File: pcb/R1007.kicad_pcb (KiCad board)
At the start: 4 copper layers, 69 x 38.6 mm, 36 parts, among them J1 CONN500P-01X08, J2 CONN500P-01X08, J3 CONN_R1000A_EXTENSION, Q1 PSMN1R2-30YLC, Q2 PSMN1R2-30YLC, Q3 PSMN1R2-30YLC, Q4 PSMN1R2-30YLC, U1 74HC125, U2 AS78L05ZTR-E1, U3 TLP293-4

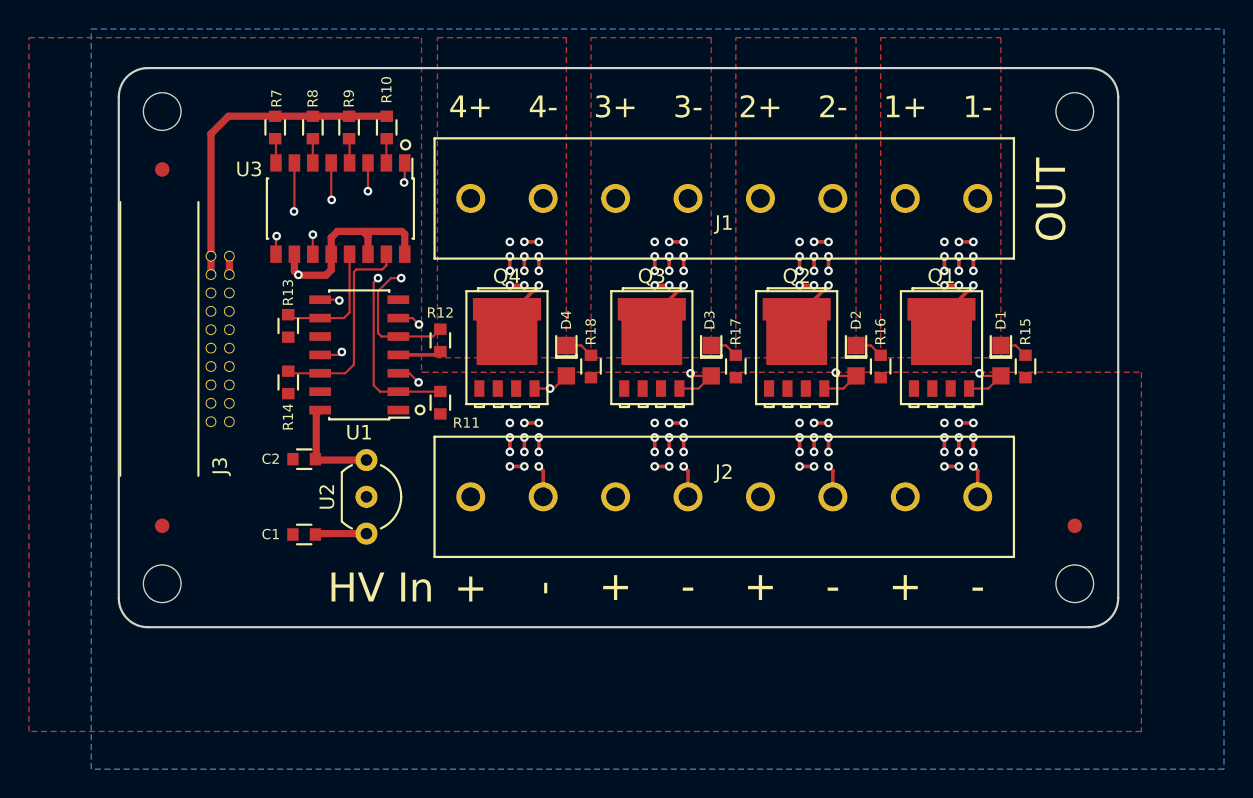
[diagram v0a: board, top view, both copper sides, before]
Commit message: separated +ve supplies and moved LEDs to board edge
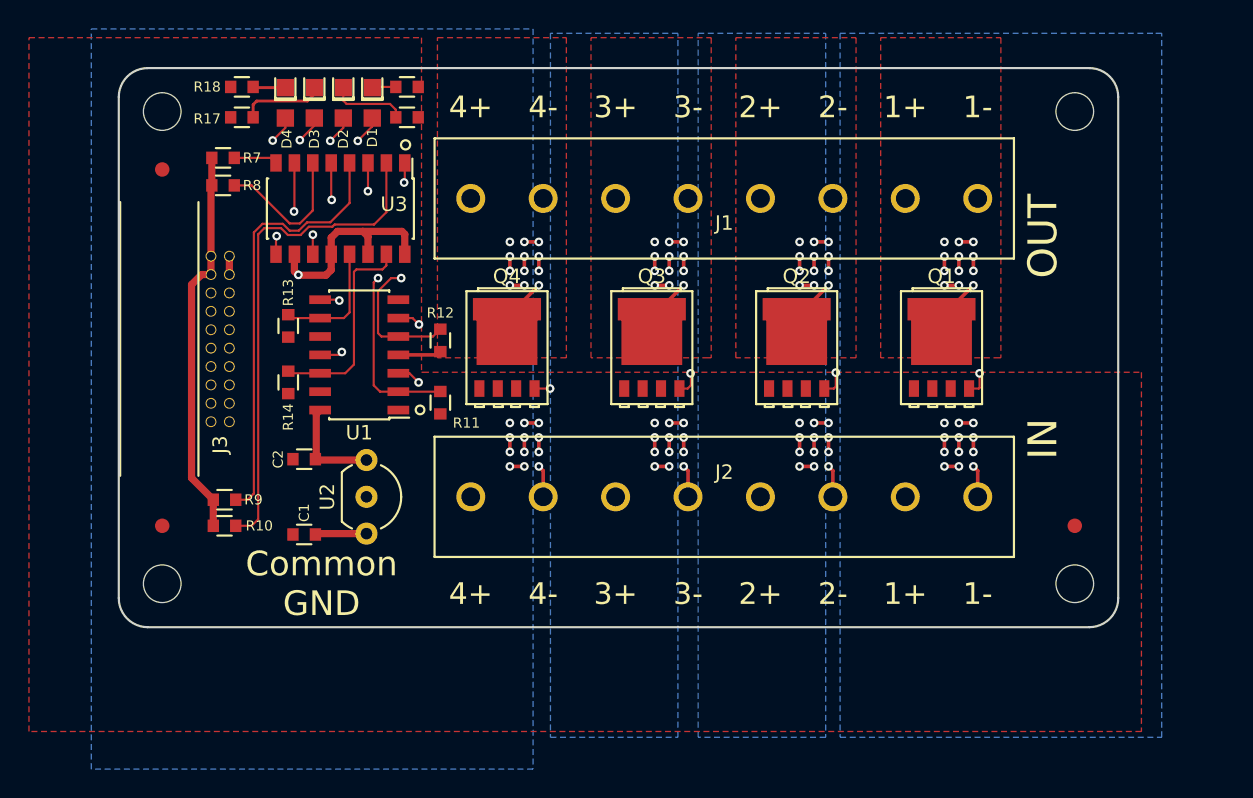
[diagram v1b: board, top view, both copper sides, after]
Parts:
- moved D1 46.9 mm to (120.5, 70.4)
- moved R15 46.9 mm to (122.9, 69.3), turned to 0 degrees
- moved D2 39.6 mm to (118.5, 70.4)
- moved R17 38.2 mm to (111.5, 71.4), turned to 180 degrees
- moved R16 36.9 mm to (122.9, 71.4), turned to 0 degrees
- moved D3 32.7 mm to (116.5, 70.4)
- moved R18 30.9 mm to (111.5, 69.3), turned to 180 degrees
- moved R10 29.7 mm to (110.3, 99.6), turned to 180 degrees
- moved R9 27.1 mm to (110.3, 97.8), turned to 180 degrees
- moved D4 26.3 mm to (114.5, 70.4)
- moved R8 7.38 mm to (110.2, 76.1), turned to 180 degrees
- moved R7 4.17 mm to (110.2, 74.2), turned to 180 degrees
- moved A1 3.00 mm to (159.4, 90.0)
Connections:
- J1 pad 2: VDD -> /VDD4
- J1 pad 4: VDD -> /VDD3
- J1 pad 6: VDD -> /VDD2
- J2 pad 3: VDD -> /VDD2
- J2 pad 5: VDD -> /VDD3
- J2 pad 7: VDD -> /VDD4
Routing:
- net /INR1: track 1.69 -> 34.7 mm
- net /INR2: track 1.69 -> 30.1 mm
- net /GN4: track 13.5 -> 39.4 mm, vias 2 -> 3
- net /GN3: track 28.2 -> 51.2 mm, vias 2 -> 3
- net /GN1: track 58.5 -> 73.2 mm, vias 2 -> 3
- net /GN2: track 43.2 -> 54.3 mm, vias 2 -> 3
- net /INR3: track 1.68 -> 10.2 mm
- net Net-(D3-Pad1): track 1.98 -> 5.85 mm
- net Net-(D2-Pad1): track 1.98 -> 5.31 mm
- net GND: track 25.0 -> 27.0 mm
- net /INR4: track 1.70 -> 3.03 mm
- added copper zone on B.Cu, net /VDD2
- added copper zone on In2.Cu, net /VDD2
- added copper zone on B.Cu, net /VDD3
- added copper zone on In2.Cu, net /VDD3
- added copper zone on B.Cu, net /VDD4
- added copper zone on In2.Cu, net /VDD4
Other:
- board text added: "Common GND"
- board text added: "IN"
- board text added: "R1007 v1.2 Quad 20A NFET Drivers plugg.ee Labs LLC http://plugg.ee"
- board text added: "Separate +VE Supplies (9 to 24V)"
- board text removed: "+"
- board text removed: "-"
- board text removed: "HV In"
- board text removed: "R1007 v1.1 Quad 20A NFET Drivers plugg.ee Labs LLC http://plugg.ee"
